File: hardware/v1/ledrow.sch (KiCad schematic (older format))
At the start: 8 parts

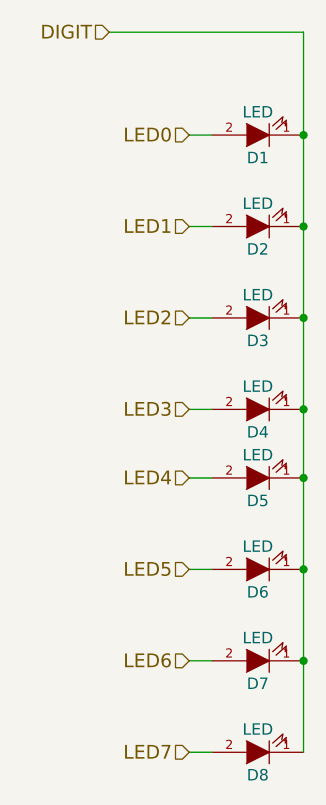
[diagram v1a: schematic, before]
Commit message: More routing experiments.
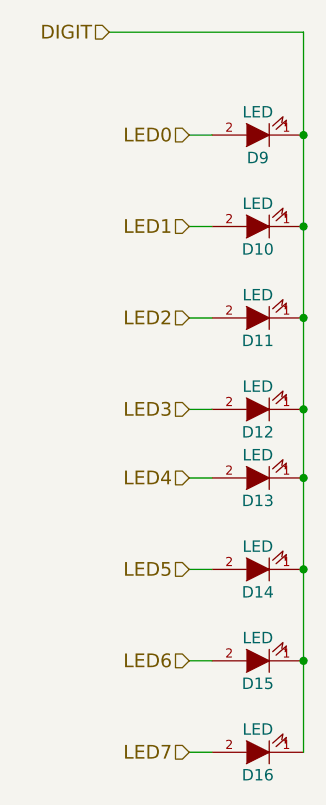
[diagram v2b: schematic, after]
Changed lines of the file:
@@
 AR Path="/57A56122/57A3F0CE/57A35AD5" Ref="D64"  Part="1"
 AR Path="/57A3E922/57A35AD5" Ref="D8"  Part="1"
-AR Path="/57A3F0CE/57A35AD5" Ref="D?"  Part="1"
-F 0 "D?" H 1800 4000 50  0000 C CNN
+AR Path="/57A3F0CE/57A35AD5" Ref="D16"  Part="1"
+F 0 "D16" H 1800 4000 50  0000 C CNN
 F 1 "LED" H 1800 3800 50  0000 C CNN
 F 2 "LEDs:LED-5MM" H 1800 3900 50  0001 C CNN
@@
 AR Path="/57A56122/57A3F0CE/57A35B88" Ref="D63"  Part="1"
 AR Path="/57A3E922/57A35B88" Ref="D7"  Part="1"
-AR Path="/57A3F0CE/57A35B88" Ref="D?"  Part="1"
-F 0 "D?" H 1800 3600 50  0000 C CNN
+AR Path="/57A3F0CE/57A35B88" Ref="D15"  Part="1"
+F 0 "D15" H 1800 3600 50  0000 C CNN
 F 1 "LED" H 1800 3400 50  0000 C CNN
 F 2 "LEDs:LED-5MM" H 1800 3500 50  0001 C CNN
@@
 AR Path="/57A56122/57A3F0CE/57A35BB5" Ref="D62"  Part="1"
 AR Path="/57A3E922/57A35BB5" Ref="D6"  Part="1"
-AR Path="/57A3F0CE/57A35BB5" Ref="D?"  Part="1"
-F 0 "D?" H 1800 3200 50  0000 C CNN
+AR Path="/57A3F0CE/57A35BB5" Ref="D14"  Part="1"
+F 0 "D14" H 1800 3200 50  0000 C CNN
 F 1 "LED" H 1800 3000 50  0000 C CNN
 F 2 "LEDs:LED-5MM" H 1800 3100 50  0001 C CNN
@@
 AR Path="/57A56122/57A3F0CE/57A35BD9" Ref="D61"  Part="1"
 AR Path="/57A3E922/57A35BD9" Ref="D5"  Part="1"
-AR Path="/57A3F0CE/57A35BD9" Ref="D?"  Part="1"
-F 0 "D?" H 1800 2800 50  0000 C CNN
+AR Path="/57A3F0CE/57A35BD9" Ref="D13"  Part="1"
+F 0 "D13" H 1800 2800 50  0000 C CNN
 F 1 "LED" H 1800 2600 50  0000 C CNN
 F 2 "LEDs:LED-5MM" H 1800 2700 50  0001 C CNN
@@
 AR Path="/57A56122/57A3F0CE/57A35D11" Ref="D60"  Part="1"
 AR Path="/57A3E922/57A35D11" Ref="D4"  Part="1"
-AR Path="/57A3F0CE/57A35D11" Ref="D?"  Part="1"
-F 0 "D?" H 1800 2500 50  0000 C CNN
+AR Path="/57A3F0CE/57A35D11" Ref="D12"  Part="1"
+F 0 "D12" H 1800 2500 50  0000 C CNN
 F 1 "LED" H 1800 2300 50  0000 C CNN
 F 2 "LEDs:LED-5MM" H 1800 2400 50  0001 C CNN
@@
 AR Path="/57A56122/57A3F0CE/57A35D17" Ref="D59"  Part="1"
 AR Path="/57A3E922/57A35D17" Ref="D3"  Part="1"
-AR Path="/57A3F0CE/57A35D17" Ref="D?"  Part="1"
-F 0 "D?" H 1800 2100 50  0000 C CNN
+AR Path="/57A3F0CE/57A35D17" Ref="D11"  Part="1"
+F 0 "D11" H 1800 2100 50  0000 C CNN
 F 1 "LED" H 1800 1900 50  0000 C CNN
 F 2 "LEDs:LED-5MM" H 1800 2000 50  0001 C CNN
@@
 AR Path="/57A56122/57A3F0CE/57A35D1D" Ref="D58"  Part="1"
 AR Path="/57A3E922/57A35D1D" Ref="D2"  Part="1"
-AR Path="/57A3F0CE/57A35D1D" Ref="D?"  Part="1"
-F 0 "D?" H 1800 1700 50  0000 C CNN
+AR Path="/57A3F0CE/57A35D1D" Ref="D10"  Part="1"
+F 0 "D10" H 1800 1700 50  0000 C CNN
 F 1 "LED" H 1800 1500 50  0000 C CNN
 F 2 "LEDs:LED-5MM" H 1800 1600 50  0001 C CNN
@@
 AR Path="/57A56122/57A3F0CE/57A35D23" Ref="D57"  Part="1"
 AR Path="/57A3E922/57A35D23" Ref="D1"  Part="1"
-AR Path="/57A3F0CE/57A35D23" Ref="D?"  Part="1"
-F 0 "D?" H 1800 1300 50  0000 C CNN
+AR Path="/57A3F0CE/57A35D23" Ref="D9"  Part="1"
+F 0 "D9" H 1800 1300 50  0000 C CNN
 F 1 "LED" H 1800 1100 50  0000 C CNN
 F 2 "LEDs:LED-5MM" H 1800 1200 50  0001 C CNN

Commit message: Manually route lmaps-16 board
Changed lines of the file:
@@
 LIBS:contrib
 LIBS:valves
+LIBS:lamps-16-cache
 EELAYER 25 0
 EELAYER END
@@
 Date ""
 Rev ""
-Comp ""
-Comment1 ""
+Comp "University of Glasgow"
+Comment1 "Kristian Hentschel"
 Comment2 ""
 Comment3 ""
-Comment4 ""
+Comment4 "REDEUCE Control Panel"
 $EndDescr
 $Comp
@@
 AR Path="/57A3E922/57A35AD5" Ref="D8"  Part="1"
 AR Path="/57A3F0CE/57A35AD5" Ref="D16"  Part="1"
-F 0 "D16" H 1800 4000 50  0000 C CNN
+F 0 "D8" H 1800 4000 50  0000 C CNN
 F 1 "LED" H 1800 3800 50  0000 C CNN
 F 2 "LEDs:LED-5MM" H 1800 3900 50  0001 C CNN
@@
 AR Path="/57A3E922/57A35B88" Ref="D7"  Part="1"
 AR Path="/57A3F0CE/57A35B88" Ref="D15"  Part="1"
-F 0 "D15" H 1800 3600 50  0000 C CNN
+F 0 "D7" H 1800 3600 50  0000 C CNN
 F 1 "LED" H 1800 3400 50  0000 C CNN
 F 2 "LEDs:LED-5MM" H 1800 3500 50  0001 C CNN
@@
 AR Path="/57A3E922/57A35BB5" Ref="D6"  Part="1"
 AR Path="/57A3F0CE/57A35BB5" Ref="D14"  Part="1"
-F 0 "D14" H 1800 3200 50  0000 C CNN
+F 0 "D6" H 1800 3200 50  0000 C CNN
 F 1 "LED" H 1800 3000 50  0000 C CNN
 F 2 "LEDs:LED-5MM" H 1800 3100 50  0001 C CNN
@@
 AR Path="/57A3E922/57A35BD9" Ref="D5"  Part="1"
 AR Path="/57A3F0CE/57A35BD9" Ref="D13"  Part="1"
-F 0 "D13" H 1800 2800 50  0000 C CNN
+F 0 "D5" H 1800 2800 50  0000 C CNN
 F 1 "LED" H 1800 2600 50  0000 C CNN
 F 2 "LEDs:LED-5MM" H 1800 2700 50  0001 C CNN
@@
 AR Path="/57A3E922/57A35D11" Ref="D4"  Part="1"
 AR Path="/57A3F0CE/57A35D11" Ref="D12"  Part="1"
-F 0 "D12" H 1800 2500 50  0000 C CNN
+F 0 "D4" H 1800 2500 50  0000 C CNN
 F 1 "LED" H 1800 2300 50  0000 C CNN
 F 2 "LEDs:LED-5MM" H 1800 2400 50  0001 C CNN
@@
 AR Path="/57A3E922/57A35D17" Ref="D3"  Part="1"
 AR Path="/57A3F0CE/57A35D17" Ref="D11"  Part="1"
-F 0 "D11" H 1800 2100 50  0000 C CNN
+F 0 "D3" H 1800 2100 50  0000 C CNN
 F 1 "LED" H 1800 1900 50  0000 C CNN
 F 2 "LEDs:LED-5MM" H 1800 2000 50  0001 C CNN
@@
 AR Path="/57A3E922/57A35D1D" Ref="D2"  Part="1"
 AR Path="/57A3F0CE/57A35D1D" Ref="D10"  Part="1"
-F 0 "D10" H 1800 1700 50  0000 C CNN
+F 0 "D2" H 1800 1700 50  0000 C CNN
 F 1 "LED" H 1800 1500 50  0000 C CNN
 F 2 "LEDs:LED-5MM" H 1800 1600 50  0001 C CNN
@@
 AR Path="/57A3E922/57A35D23" Ref="D1"  Part="1"
 AR Path="/57A3F0CE/57A35D23" Ref="D9"  Part="1"
-F 0 "D9" H 1800 1300 50  0000 C CNN
+F 0 "D1" H 1800 1300 50  0000 C CNN
 F 1 "LED" H 1800 1100 50  0000 C CNN
 F 2 "LEDs:LED-5MM" H 1800 1200 50  0001 C CNN
